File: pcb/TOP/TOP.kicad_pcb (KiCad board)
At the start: 2 copper layers, 52 x 63 mm, 95 parts, among them J1 Conn_01x04, Q1 BF545A, Q2 BF545A, U1 ICL7660, U2 L78L15_SOT89, U3 TL074, U4 OPA2604

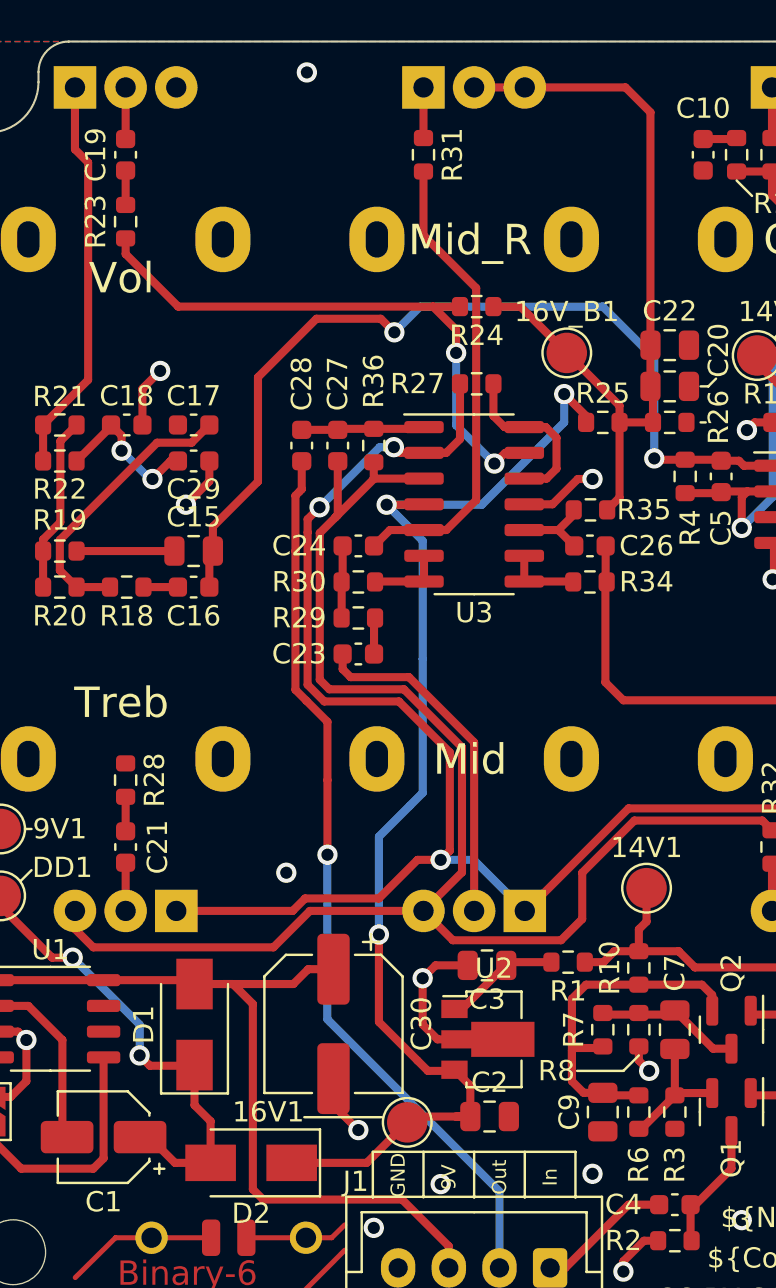
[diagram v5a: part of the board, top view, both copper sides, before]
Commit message: [TOP] Run and fix DRC
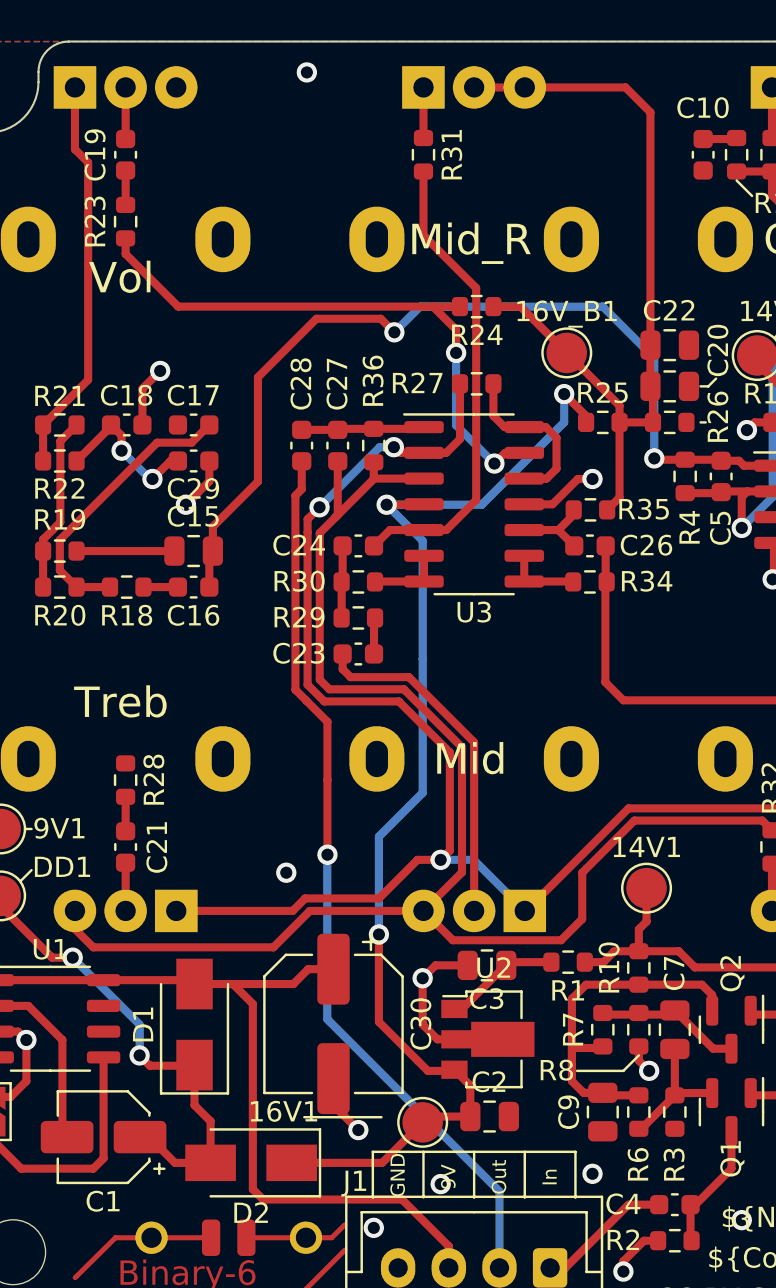
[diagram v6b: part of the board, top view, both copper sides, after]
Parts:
- moved 16V1 0.76 mm to (147.0, 120.8)
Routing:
- net +16V: track 60.6 -> 59.8 mm
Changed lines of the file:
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@@
   )
   (footprint "TestPoint:TestPoint_Pad_D2.0mm" (layer "F.Cu")
-    (at 146.198 120.84)
+    (at 146.96 120.84)
     (descr "SMD pad as test Point, diameter 2.0mm")
     (tags "test point SMD pad")
@@
   (segment (start 132.3 73.863) (end 132.3 75.565) (width 0.4) (layer "F.Cu") (net 26))
   (segment (start 132.3 72.313) (end 132.3 69.765) (width 0.4) (layer "F.Cu") (net 27))
-  (segment (start 132.355 69.82) (end 132.3 69.765) (width 0.4) (layer "F.Cu") (net 27))
   (segment (start 156.972 69.765) (end 158.202 70.995) (width 0.4) (layer "F.Cu") (net 28))
   (segment (start 150.452 80.581) (end 151.786 80.581) (width 0.4) (layer "F.Cu") (net 28))
@@
   (segment (start 156.675 85.47) (end 154.072 82.867) (width 0.4) (layer "F.Cu") (net 28))
   (segment (start 156.675 90.0044) (end 156.675 86.296) (width 0.4) (layer "F.Cu") (net 28))
-  (segment (start 158.075 82.613) (end 158.202 82.486) (width 0.4) (layer "F.Cu") (net 28))
   (segment (start 156.675 86.296) (end 158.327 86.296) (width 0.4) (layer "F.Cu") (net 28))
   (segment (start 156.0654 90.614) (end 156.675 90.0044) (width 0.4) (layer "F.Cu") (net 28))
@@
   (segment (start 154.369 94.149) (end 154.39 94.17) (width 0.4) (layer "F.Cu") (net 49))
   (segment (start 151.975 94.149) (end 154.369 94.149) (width 0.4) (layer "F.Cu") (net 49))
-  (segment (start 144.198 122.84) (end 146.198 120.84) (width 0.4) (layer "F.Cu") (net 53))
-  (segment (start 149.312 120.554) (end 146.484 120.554) (width 0.4) (layer "F.Cu") (net 53))
   (segment (start 146.706 117.792) (end 147.214 118.3) (width 0.4) (layer "F.Cu") (net 53))
   (segment (start 144.801 115.887) (end 144.801 111.569) (width 0.4) (layer "F.Cu") (net 53))
@@
   (segment (start 147.004 90.36) (end 147.025 90.339) (width 0.4) (layer "F.Cu") (net 53))
   (segment (start 148.472 118.3) (end 148.528 118.244) (width 0.4) (layer "F.Cu") (net 53))
-  (segment (start 146.484 120.554) (end 146.198 120.84) (width 0.4) (layer "F.Cu") (net 53))
   (segment (start 145.182 90.36) (end 147.004 90.36) (width 0.4) (layer "F.Cu") (net 53))
+  (segment (start 144.96 122.84) (end 146.96 120.84) (width 0.4) (layer "F.Cu") (net 53))
   (segment (start 147.214 118.3) (end 148.472 118.3) (width 0.4) (layer "F.Cu") (net 53))
   (segment (start 155.025 85.979) (end 155.025 86.296) (width 0.4) (layer "F.Cu") (net 53))
-  (segment (start 148.59 120.554) (end 149.312 120.554) (width 0.4) (layer "F.Cu") (net 53))
-  (segment (start 140.494 122.84) (end 144.198 122.84) (width 0.4) (layer "F.Cu") (net 53))
+  (segment (start 147.246 120.554) (end 146.96 120.84) (width 0.4) (layer "F.Cu") (net 53))
   (segment (start 149.312 120.554) (end 149.312 119.028) (width 0.4) (layer "F.Cu") (net 53))
+  (segment (start 140.494 122.84) (end 144.96 122.84) (width 0.4) (layer "F.Cu") (net 53))
   (segment (start 146.706 117.792) (end 144.801 115.887) (width 0.4) (layer "F.Cu") (net 53))
+  (segment (start 149.312 120.554) (end 147.246 120.554) (width 0.4) (layer "F.Cu") (net 53))
   (via (at 144.801 111.569) (size 1) (drill 0.6) (layers "F.Cu" "B.Cu") (net 53))
   (via (at 145.182 90.36) (size 1) (drill 0.6) (layers "F.Cu" "B.Cu") (net 53))

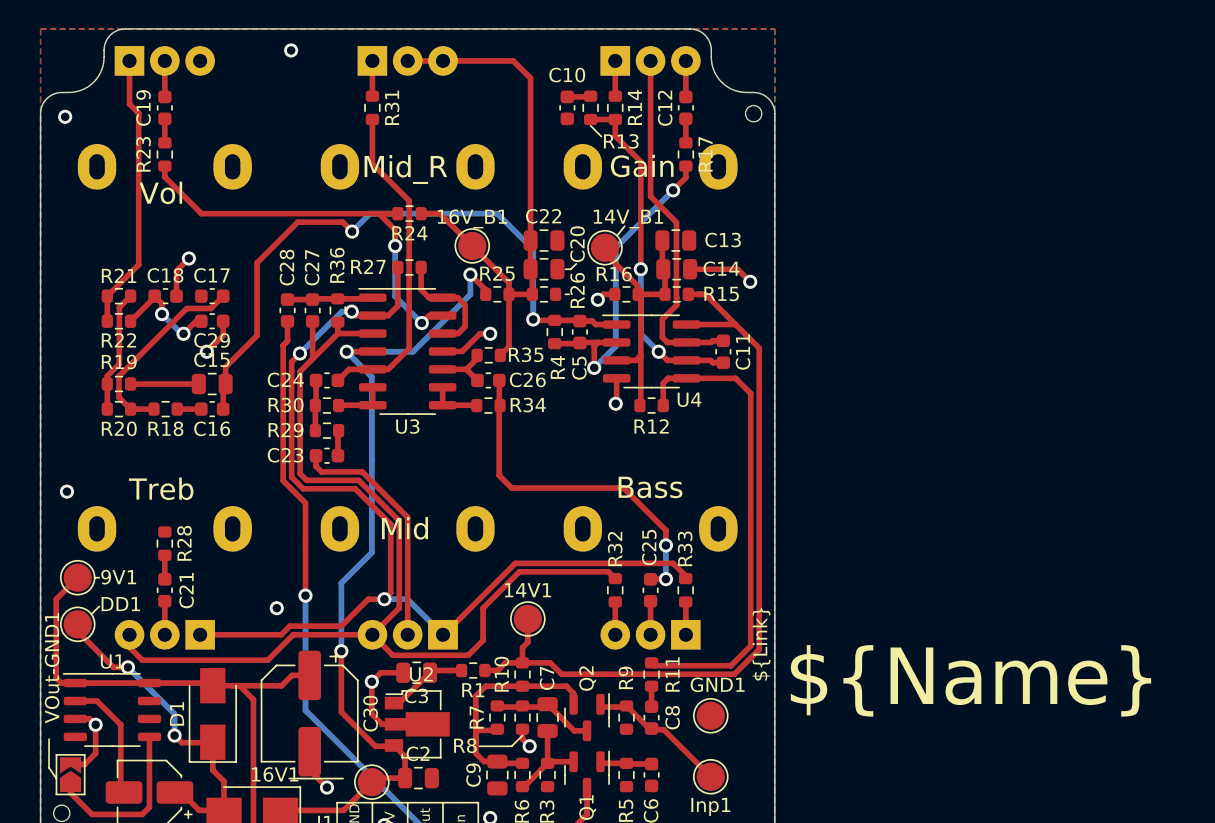
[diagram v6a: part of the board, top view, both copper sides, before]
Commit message: [TOP] Optimize silkscreen designs
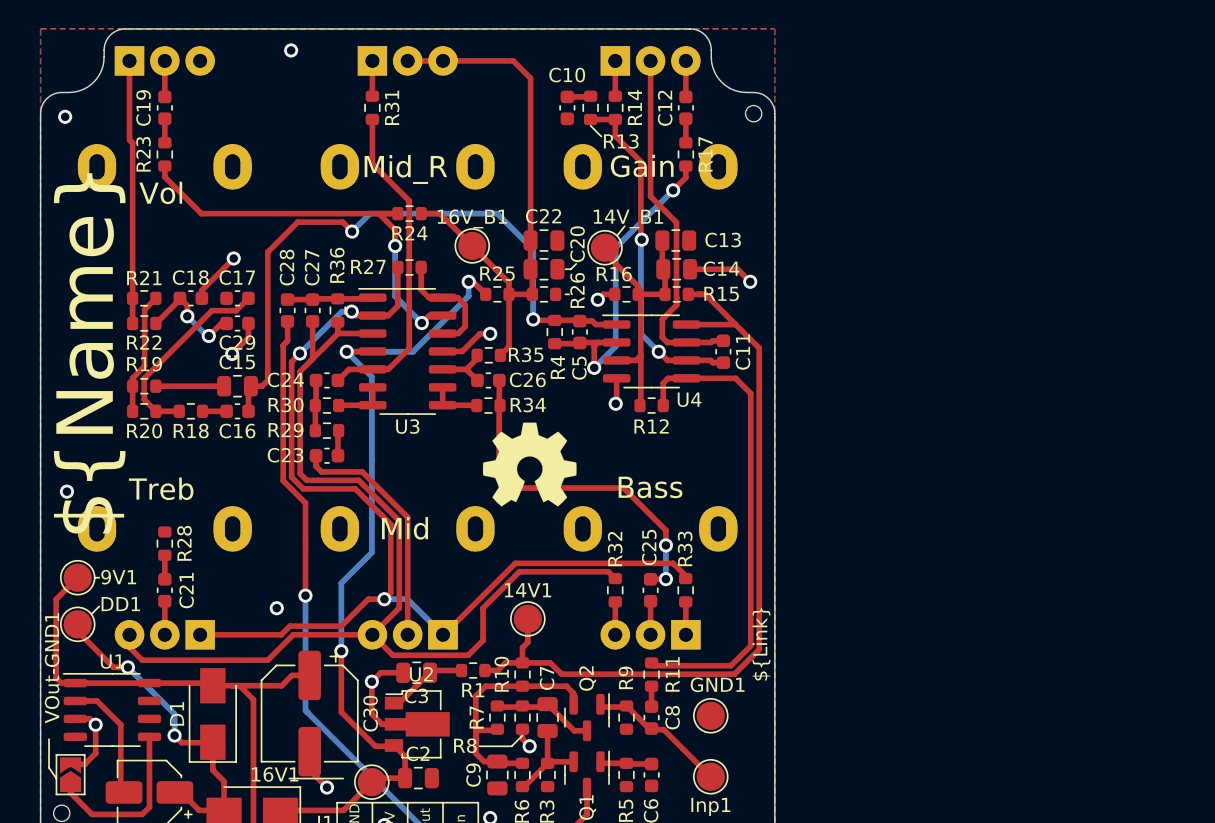
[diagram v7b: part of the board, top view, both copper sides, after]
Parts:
- added REF**: OSHW-Symbol_6.7x6mm_SilkScreen, Symbol:OSHW-Symbol_6.7x6mm_SilkScreen, F.Cu at (158.1, 98.4)
- added REF**: OSHW-Symbol_6.7x6mm_SilkScreen, Symbol:OSHW-Symbol_6.7x6mm_SilkScreen, B.Cu at (137.3, 119.1)
- moved C18 1.80 mm to (134.1, 86.6)
- moved R19 1.80 mm to (130.8, 92.8)
- moved R21 1.80 mm to (130.8, 86.6)
- moved R22 1.80 mm to (130.8, 88.4)
- moved R18 1.80 mm to (134.1, 94.6)
- moved R20 1.80 mm to (130.8, 94.6)
- moved C15 1.80 mm to (137.4, 92.8)
- moved C17 1.80 mm to (137.4, 86.6)
- moved C29 1.80 mm to (137.4, 88.4)
- moved C16 1.80 mm to (137.4, 94.6)
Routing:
- net +16V: track 59.8 -> 59.0 mm
- net GND: track 37.1 -> 37.8 mm
- net Net-(R21-Pad2): track 19.6 -> 19.0 mm

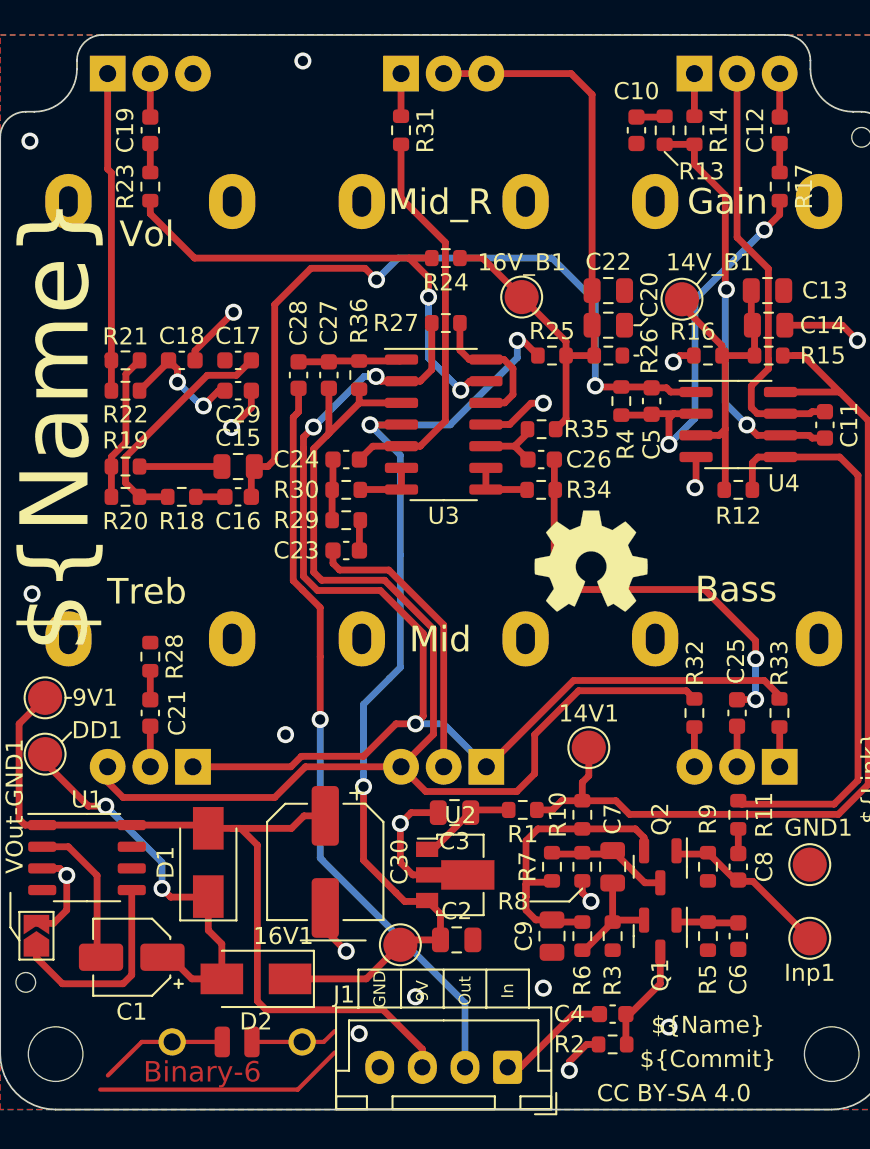
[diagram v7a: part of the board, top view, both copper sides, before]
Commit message: [TOP] Optimize some tracks and pours
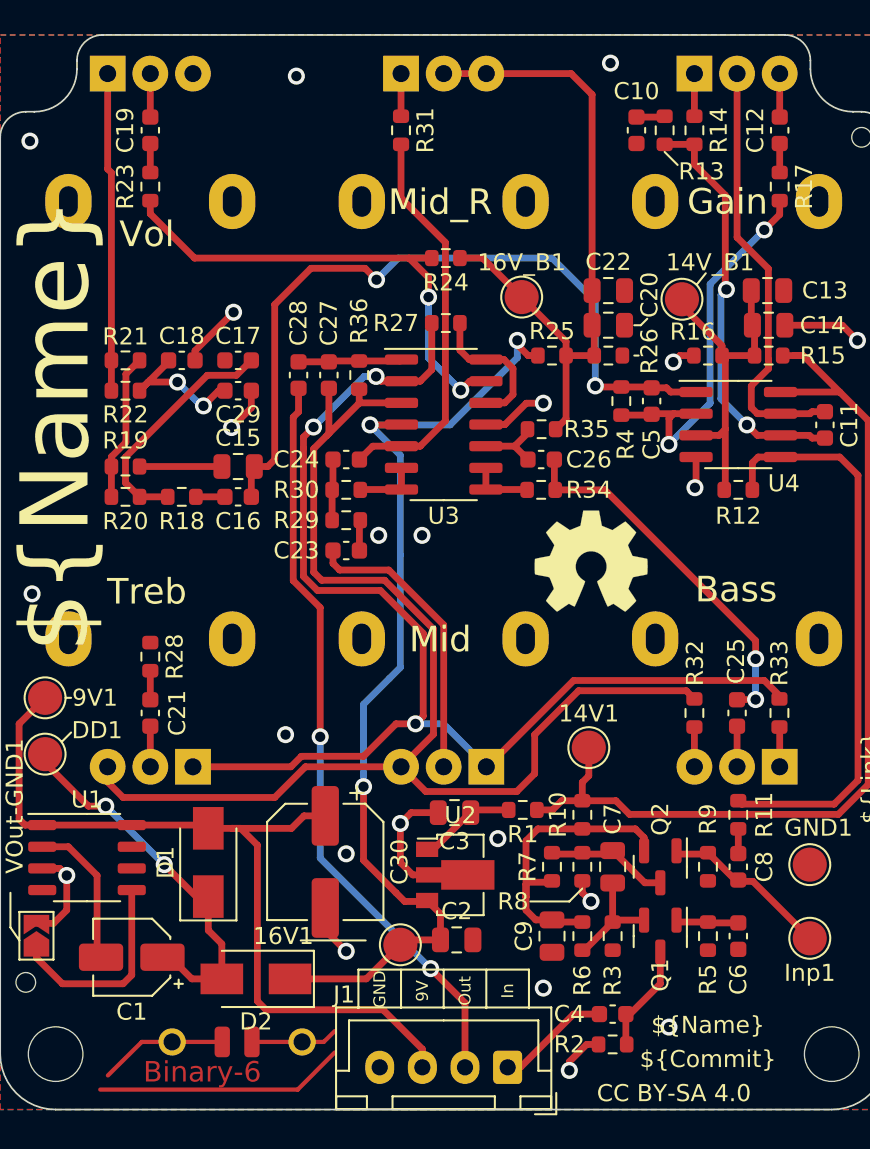
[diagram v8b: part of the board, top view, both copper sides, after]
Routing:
- net Net-(C25-Pad1): track 24.7 -> 21.8 mm
- net Net-(C18-Pad1): track 7.70 -> 8.64 mm
- net Net-(C1-Pad1): track 23.4 -> 22.5 mm
- net Upper_PCB_Output: track 44.2 -> 44.1 mm, vias 1 -> 2
- net GND: vias 19 -> 22
